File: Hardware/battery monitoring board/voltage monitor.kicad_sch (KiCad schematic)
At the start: 10 parts, among them J1 S5B-XH-A

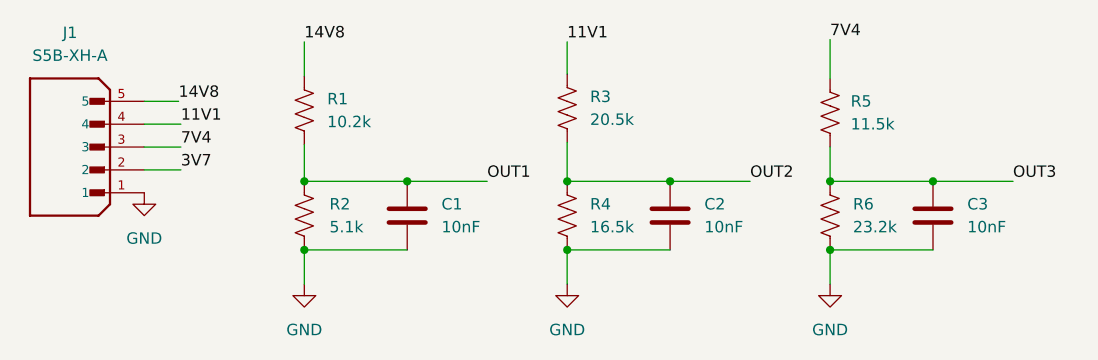
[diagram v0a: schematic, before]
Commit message: Added hiearchical labels to battery monitoring sheets
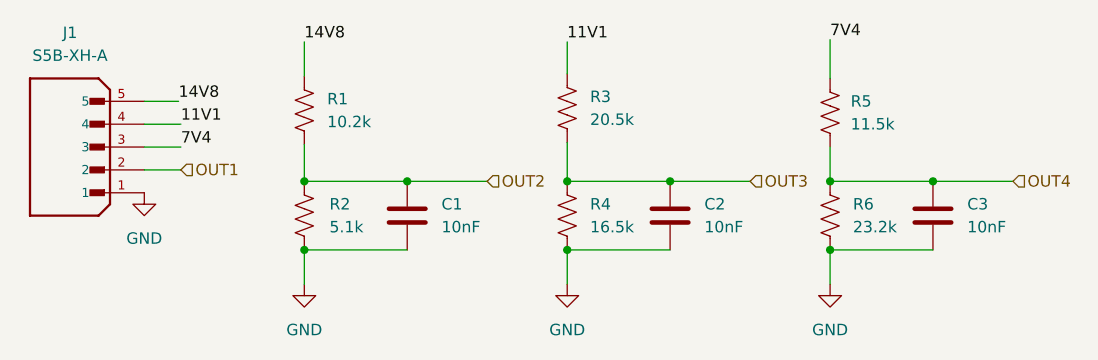
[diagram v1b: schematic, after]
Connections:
- net 3V7 is gone; now on net OUT1: J1.2
- net OUT1: no longer C1.1, R1.1, R2.2
- net OUT2: now also C1.1, R1.1, R2.2; no longer C2.1, R3.1, R4.1
- net OUT3: now also C2.1, R3.1, R4.1; no longer C3.1, R5.1, R6.1
- new net OUT4: C3.1, R5.1, R6.1
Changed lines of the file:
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@@
-    (effects (font (size 1.27 1.27)) (justify left bottom))
-  )
-  (label "OUT3" (at 128.27 35.56 0) (fields_autoplaced)
     (effects (font (size 1.27 1.27)) (justify left bottom))
   )
@@
     (effects (font (size 1.27 1.27)) (justify left bottom))
   )
-  (label "OUT1" (at 69.85 35.56 0) (fields_autoplaced)
-    (effects (font (size 1.27 1.27)) (justify left bottom))
-  )
   (label "14V8" (at 49.53 20.066 0) (fields_autoplaced)
     (effects (font (size 1.27 1.27)) (justify left bottom))
@@
     (effects (font (size 1.27 1.27)) (justify left bottom))
   )
-  (label "OUT2" (at 99.06 35.56 0) (fields_autoplaced)
-    (effects (font (size 1.27 1.27)) (justify left bottom))
-  )
-  (label "3V7" (at 35.814 34.29 0) (fields_autoplaced)
-    (effects (font (size 1.27 1.27)) (justify left bottom))
+  (hierarchical_label "OUT4" (shape input) (at 128.27 35.56 0) (fields_autoplaced)
+    (effects (font (size 1.27 1.27)) (justify left))
+  )
+  (hierarchical_label "OUT1" (shape input) (at 35.814 34.29 0) (fields_autoplaced)
+    (effects (font (size 1.27 1.27)) (justify left))
+  )
+  (hierarchical_label "OUT2" (shape input) (at 69.85 35.56 0) (fields_autoplaced)
+    (effects (font (size 1.27 1.27)) (justify left))
+  )
+  (hierarchical_label "OUT3" (shape input) (at 99.06 35.56 0) (fields_autoplaced)
+    (effects (font (size 1.27 1.27)) (justify left))
   )
   (symbol (lib_id "power:GND") (at 31.75 36.83 0) (unit 1)
@@
         )
       )
+      (project "battery monitoring board"
+        (path "/bf623d80-ca5a-491f-9daa-4dffbeba5279/986cc9e1-c37e-4aa2-b3b5-8e2dcbe750c5"
+          (reference "C3") (unit 1)
+        )
+      )
     )
   )
@@
       (project "voltage monitor"
         (path "/64dd58dd-0f80-4046-8958-33031e8c772b"
+          (reference "C1") (unit 1)
+        )
+      )
+      (project "battery monitoring board"
+        (path "/bf623d80-ca5a-491f-9daa-4dffbeba5279/986cc9e1-c37e-4aa2-b3b5-8e2dcbe750c5"
           (reference "C1") (unit 1)
         )
@@
         )
       )
+      (project "battery monitoring board"
+        (path "/bf623d80-ca5a-491f-9daa-4dffbeba5279/986cc9e1-c37e-4aa2-b3b5-8e2dcbe750c5"
+          (reference "#PWR04") (unit 1)
+        )
+      )
     )
   )
@@
         )
       )
+      (project "battery monitoring board"
+        (path "/bf623d80-ca5a-491f-9daa-4dffbeba5279/986cc9e1-c37e-4aa2-b3b5-8e2dcbe750c5"
+          (reference "#PWR02") (unit 1)
+        )
+      )
     )
   )
@@
         )
       )
+      (project "battery monitoring board"
+        (path "/bf623d80-ca5a-491f-9daa-4dffbeba5279/986cc9e1-c37e-4aa2-b3b5-8e2dcbe750c5"
+          (reference "#PWR03") (unit 1)
+        )
+      )
     )
   )
@@
           (reference "C2") (unit 1)
         )
+      )
+      (project "battery monitoring board"
+        (path "/bf623d80-ca5a-491f-9daa-4dffbeba5279/986cc9e1-c37e-4aa2-b3b5-8e2dcbe750c5"
+          (reference "C2") (unit 1)
+        )

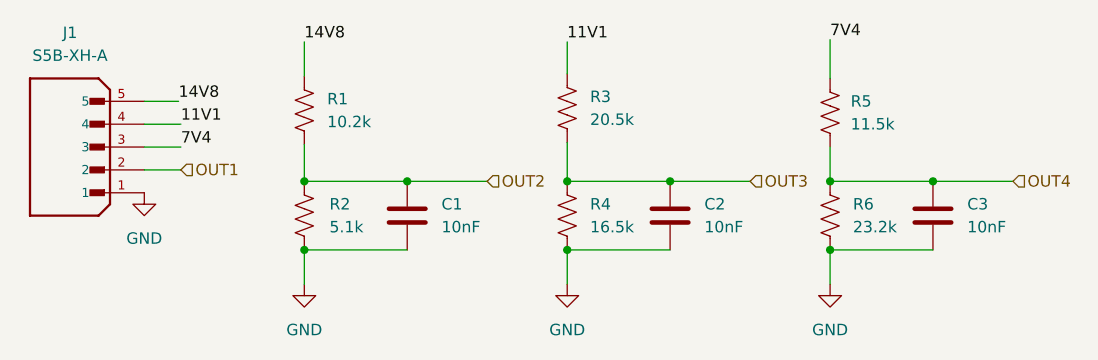
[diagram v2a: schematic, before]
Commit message: Update voltage monitor.kicad_sch
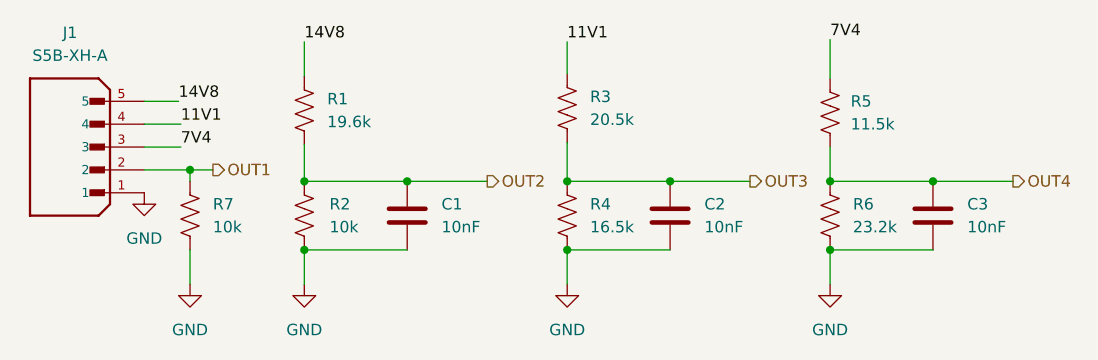
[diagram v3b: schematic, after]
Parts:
- added R7: 10k, symbol Device:R_US
- R1: value 10.2k -> 19.6k
- R2: value 5.1k -> 10k
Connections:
- net GND: now also R7.2
- net OUT1: now also R7.1
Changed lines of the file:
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@@
 (kicad_sch (version 20230121) (generator eeschema)
   (paper "A4")
+  (junction (at 36.83 34.29) (diameter 0) (color 0 0 0 0)
+  )
   (junction (at 78.74 43.18) (diameter 0) (color 0 0 0 0)
   )
@@
   (junction (at 90.17 35.56) (diameter 0) (color 0 0 0 0)
   )
+  (wire (pts (xy 36.83 43.18) (xy 36.83 46.99))
+    (stroke (width 0) (type default))
+  )
   (wire (pts (xy 31.75 31.75) (xy 35.814 31.75))
     (stroke (width 0) (type default))
@@
     (stroke (width 0) (type default))
   )
-  (wire (pts (xy 31.75 34.29) (xy 35.814 34.29))
+  (wire (pts (xy 31.75 34.29) (xy 36.83 34.29))
     (stroke (width 0) (type default))
   )
@@
     (stroke (width 0) (type default))
   )
+  (wire (pts (xy 36.83 34.29) (xy 39.37 34.29))
+    (stroke (width 0) (type default))
+  )
   (wire (pts (xy 107.95 31.75) (xy 107.95 35.56))
     (stroke (width 0) (type default))
   )
   (wire (pts (xy 49.53 35.56) (xy 60.96 35.56))
+    (stroke (width 0) (type default))
+  )
+  (wire (pts (xy 36.83 34.29) (xy 36.83 35.56))
     (stroke (width 0) (type default))
   )
@@
     (effects (font (size 1.27 1.27)) (justify left bottom))
   )
-  (hierarchical_label "OUT4" (shape input) (at 128.27 35.56 0) (fields_autoplaced)
+  (hierarchical_label "OUT4" (shape output) (at 128.27 35.56 0) (fields_autoplaced)
     (effects (font (size 1.27 1.27)) (justify left))
   )
-  (hierarchical_label "OUT1" (shape input) (at 35.814 34.29 0) (fields_autoplaced)
+  (hierarchical_label "OUT1" (shape output) (at 39.37 34.29 0) (fields_autoplaced)
     (effects (font (size 1.27 1.27)) (justify left))
   )
-  (hierarchical_label "OUT2" (shape input) (at 69.85 35.56 0) (fields_autoplaced)
+  (hierarchical_label "OUT2" (shape output) (at 69.85 35.56 0) (fields_autoplaced)
     (effects (font (size 1.27 1.27)) (justify left))
   )
-  (hierarchical_label "OUT3" (shape input) (at 99.06 35.56 0) (fields_autoplaced)
+  (hierarchical_label "OUT3" (shape output) (at 99.06 35.56 0) (fields_autoplaced)
     (effects (font (size 1.27 1.27)) (justify left))
+  )
+  (symbol (lib_id "Device:R_US") (at 36.83 39.37 0) (unit 1)
+    (in_bom yes) (on_board yes) (dnp no) (fields_autoplaced)
+    (property "Reference" "R7" (at 39.37 38.1 0)
+      (effects (font (size 1.27 1.27)) (justify left))
+    )
+    (property "Value" "10k" (at 39.37 40.64 0)
+      (effects (font (size 1.27 1.27)) (justify left))
+    )
+    (property "Footprint" "" (at 37.846 39.624 90)
+      (effects (font (size 1.27 1.27)) hide)
+    )
+    (property "Datasheet" "~" (at 36.83 39.37 0)
+      (effects (font (size 1.27 1.27)) hide)
+    )
+    (pin "1")
+    (pin "2")
+    (instances
+      (project "voltage monitor"
+        (path "/64dd58dd-0f80-4046-8958-33031e8c772b"
+          (reference "R7") (unit 1)
+        )
+      )
+    )
   )
   (symbol (lib_id "power:GND") (at 31.75 36.83 0) (unit 1)
@@
       (effects (font (size 1.27 1.27)) (justify right))
     )
-    (property "Value" "5.1k" (at 52.324 40.64 0)
+    (property "Value" "10k" (at 52.324 40.64 0)
       (effects (font (size 1.27 1.27)) (justify right))
     )
@@
       (effects (font (size 1.27 1.27)) (justify right))
     )
-    (property "Value" "10.2k" (at 52.07 28.956 0)
+    (property "Value" "19.6k" (at 52.07 28.956 0)
       (effects (font (size 1.27 1.27)) (justify right))
     )
@@
         )
       )
+    )
+  )
+  (symbol (lib_id "power:GND") (at 36.83 46.99 0) (unit 1)
+    (in_bom yes) (on_board yes) (dnp no) (fields_autoplaced)
+    (property "Reference" "#PWR05" (at 36.83 53.34 0)
+      (effects (font (size 1.27 1.27)) hide)
+    )
+    (property "Value" "GND" (at 36.83 52.07 0)
+      (effects (font (size 1.27 1.27)))
+    )
+    (property "Footprint" "" (at 36.83 46.99 0)
+      (effects (font (size 1.27 1.27)) hide)
+    )
+    (property "Datasheet" "" (at 36.83 46.99 0)
+      (effects (font (size 1.27 1.27)) hide)
+    )
+    (pin "1")
+    (instances
+      (project "voltage monitor"
+        (path "/64dd58dd-0f80-4046-8958-33031e8c772b"
+          (reference "#PWR05") (unit 1)
+        )
+      )
